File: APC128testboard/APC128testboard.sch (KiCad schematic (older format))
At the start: 62 parts, among them CON1 BARREL_JACK, J1 RJ45, P1 SPYPAD, P10 SPYPAD, P11 SPYPAD, P12 SPYPAD, P13 SPYPAD, P14 SPYPAD, P15 SPYPAD, P16 SPYPAD, P17 SPYPAD, P19 SPYPAD, P2 FPGA_CONN, P3 SPYPAD, P4 SPYPAD, P5 SPYPAD, P6 SPYPAD, P7 SPYPAD, P8 SPYPAD, P9 SPYPAD, SW1 SWITCH_INV, SW2 SWITCH_INV, SW3 SWITCH_INV, SW4 SWITCH_INV, SW5 SWITCH_INV, U1 APC128, U2 ADA4932-1, U3 LT1761, U4 AD5334, U5 LT1761

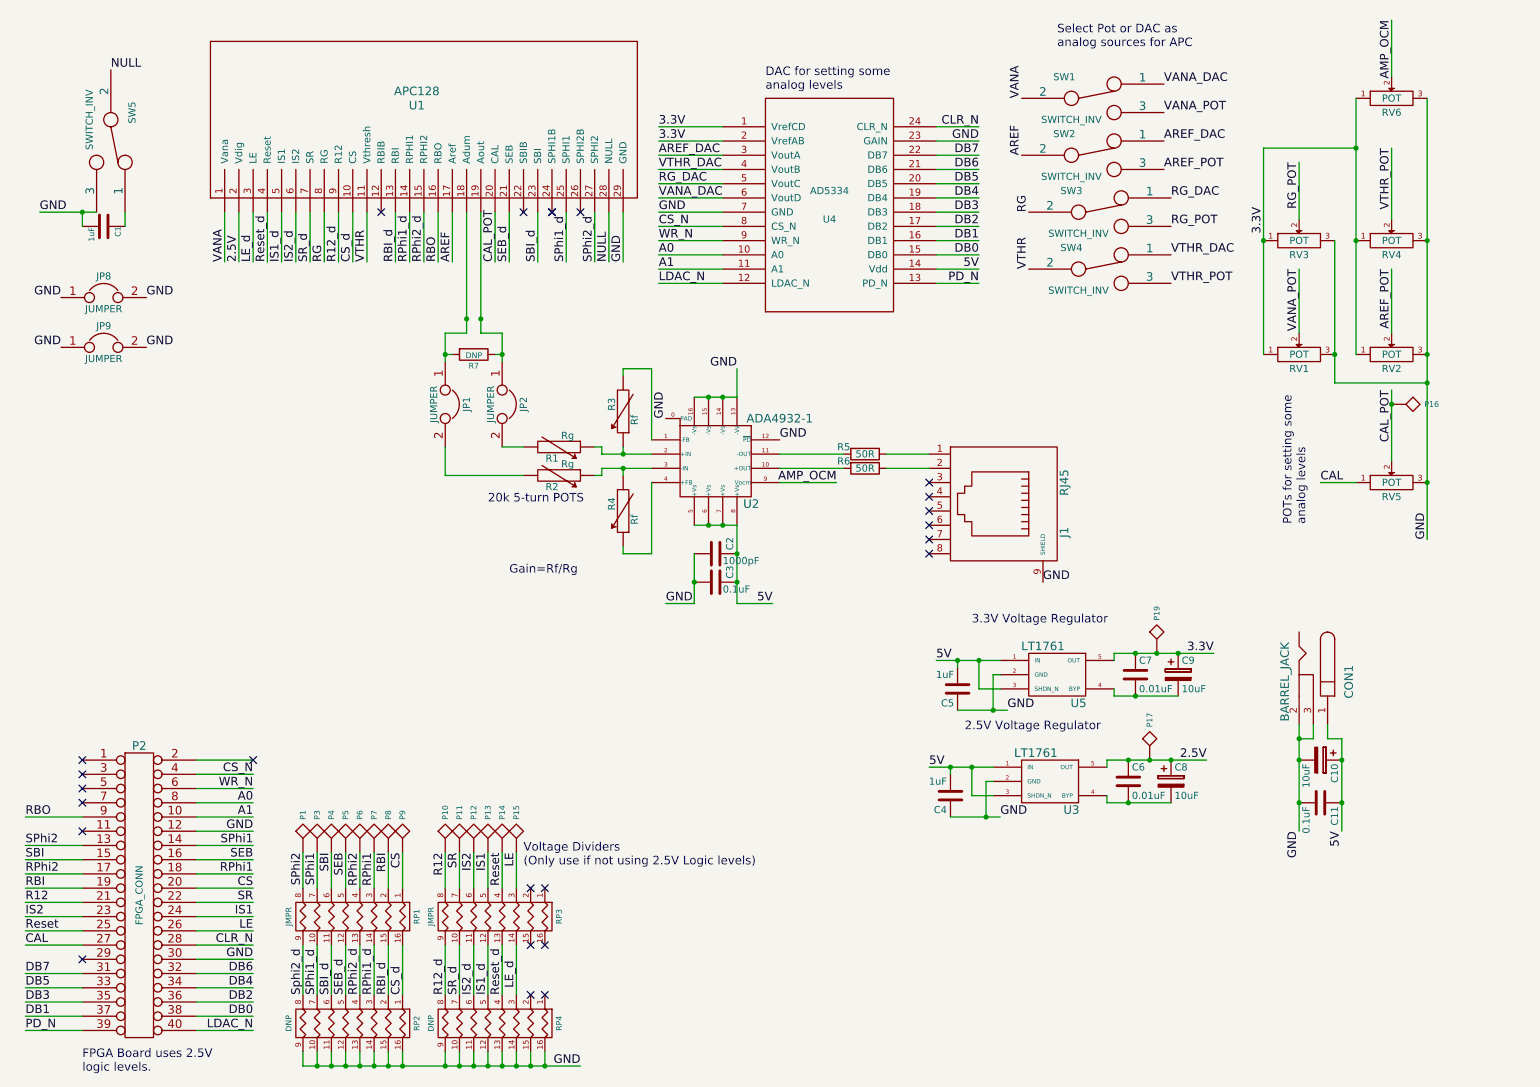
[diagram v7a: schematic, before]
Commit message: Updates APC128Testboard to revision 2
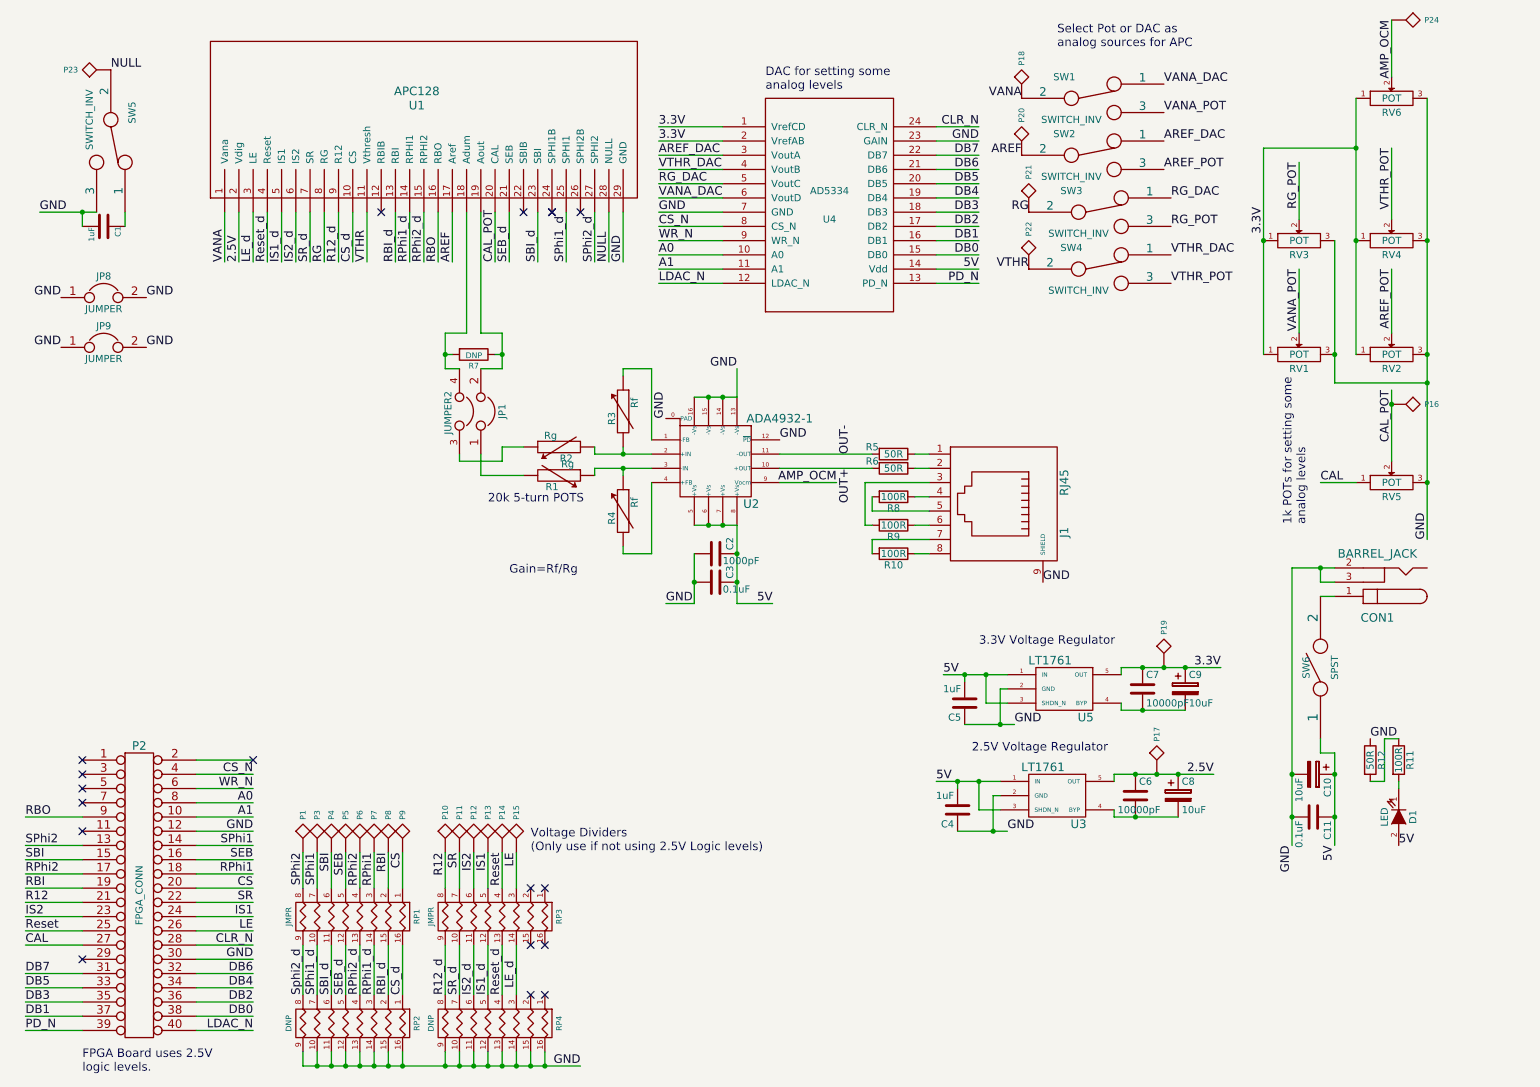
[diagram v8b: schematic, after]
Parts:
- removed JP1, JP2: JUMPER, Pin_Headers:Pin_Header_Straight_1x02, symbol JUMPER
- added D1: LED, LEDs:LED-1206, symbol LED
- added JP1: JUMPER2, extras:2x2_05Header, symbol JUMPER2
- added P18, P20, P21, P22, P23, P24: SPYPAD, extras:testpad, symbol SPYPAD
- added R10, R11, R8, R9: 100R, Resistors_SMD:R_0603, symbol R
- added R12: 50R, Resistors_SMD:R_0603, symbol R
- added SW6: SPST, extras:Switch_ES02MSABE, symbol SPST
- C1, C11, C2, C3, C4, C5: footprint SMD_Packages:SMD-0603 -> Capacitors_SMD:C_0603
- C6, C7: value 0.01uF -> 10000pF; footprint SMD_Packages:SMD-0603 -> Capacitors_SMD:C_0603
- R5, R6: footprint SMD_Packages:SMD-0603 -> Resistors_SMD:R_0603
- R7: footprint SMD_Packages:SMD-0603 -> Resistors_SMD:R_0603_HandSoldering
- RV1, RV2, RV3, RV4: footprint extras:Pot-Bourns3310Y -> extras:SM31TW+0805
- U1: footprint APC128:APC128 -> extras:APC128
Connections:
- net 5V: now also D1.2 (A), SW6.1; no longer CON1.1
- net AMP_OCM: now also P24.1
- net AREF: now also P20.1
- net GND: now also R12.1
- net NULL: now also P23.1
- net RG: now also P21.1
- net VANA: now also P18.1
- net VTHR: now also P22.1
- net at R7.2, U1.18 (Adum): now also JP1.4
- net at R7.1, U1.19 (Aout): now also JP1.2
- net at R2.2: now also R3.2, U2.2 (+IN)
- net at R1.2: now also JP1.1
- net at U2.1 (-FB): now also R3.1; no longer R3.2
- net OUT+: now reaches R6.2, U2.10 (+OUT)
- net OUT-: now reaches R5.2, U2.11 (-OUT)
- net at R4.1: now also R1.1, U2.3 (-IN); no longer U2.4 (+FB)
- net at J1.3: now also R9.2
- net at J1.4: now also R8.1
- net at J1.5: now also R8.2
- net at J1.6: now also R9.1
- net at J1.7: now also R10.2
- net at J1.8: now also R10.1
- new net: CON1.1, SW6.2
- new net: R4.2, U2.4 (+FB)
- new net: JP1.3, R2.1
- new net: D1.1 (K), R11.2
- new net: R11.1, R12.2
- no-connect marks 24 -> 18
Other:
- note added: "1k POTs for setting some \nanalog levels"
- note removed: "POTs for setting some \nanalog levels"
- moved on the sheet: C10, C11, C4, C5, C6, C7, C8, C9, CON1, P17, P19, R1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
